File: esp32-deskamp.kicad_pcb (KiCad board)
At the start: 2 copper layers, 145.2 x 66.5 mm, 39 parts, among them J1 INPUT 00, J10 ADDITIONAL GPIO, J2 INPUT 01, J3 MUTE, J4 SLEEP, J5 PRE OUT, J6 LFE OUT, J7 INPUT SELECT, J8 MOTOR, J9 12V IN, K1 INPUT 00, K2 INPUT 01, K3 AMP MUTE, K4 AMP SLEEP, U1 ESP32 D1 MINI, U2 TSR 1-2433, U3 L9110, U4 ULN2003A

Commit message: Update esp32-deskamp.kicad_pcb
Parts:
- moved R7 51.3 mm to (147.5, 74.0), turned to -90 degrees
- moved R8 48.8 mm to (145.2, 74.0), turned to -90 degrees
- moved R9 46.4 mm to (143.0, 74.0), turned to -90 degrees
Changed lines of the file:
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@@
 	(footprint "Resistor_SMD:R_0805_2012Metric_Pad1.20x1.40mm_HandSolder"
 		(layer "F.Cu")
-		(at 96.75 81.75 180)
+		(at 147.5 74 -90)
 		(descr "Resistor SMD 0805 (2012 Metric), square (rectangular) end terminal, IPC-7351 nominal with elongated pad for handsoldering. (Body size source: IPC-SM-782 page 72, https://www.pcb-3d.com/wordpress/wp-content/uploads/ipc-sm-782a_amendment_1_and_2.pdf), generated with kicad-footprint-generator")
 		(tags "resistor handsolder")
 		(property "Reference" "R7"
-			(at 0 -1.65 0)
+			(at 0 -1.65 90)
 			(layer "F.SilkS")
 			(hide yes)
@@
 		)
 		(property "Value" "10K"
-			(at 0 1.875 0)
+			(at 0 1.875 90)
 			(layer "F.SilkS")
 			(hide yes)
@@
 		)
 		(property "Datasheet" ""
-			(at 0 0 0)
+			(at 0 0 90)
 			(layer "F.Fab")
 			(hide yes)
@@
 		)
 		(property "Description" "Resistor"
-			(at 0 0 0)
+			(at 0 0 90)
 			(layer "F.Fab")
 			(hide yes)
@@
 		)
 		(fp_line
-			(start 1.85 0.95)
-			(end -1.85 0.95)
+			(start -1.85 0.95)
+			(end -1.85 -0.95)
 			(stroke
 				(width 0.05)
@@
 		)
 		(fp_line
-			(start 1.85 -0.95)
-			(end 1.85 0.95)
+			(start 1.85 0.95)
+			(end -1.85 0.95)
 			(stroke
 				(width 0.05)
@@
 		)
 		(fp_line
-			(start -1.85 0.95)
-			(end -1.85 -0.95)
+			(start -1.85 -0.95)
+			(end 1.85 -0.95)
 			(stroke
 				(width 0.05)
@@
 		)
 		(fp_line
-			(start -1.85 -0.95)
-			(end 1.85 -0.95)
+			(start 1.85 -0.95)
+			(end 1.85 0.95)
 			(stroke
 				(width 0.05)
@@
 		)
 		(fp_line
-			(start 1 0.625)
-			(end -1 0.625)
+			(start -1 0.625)
+			(end -1 -0.625)
 			(stroke
 				(width 0.1)
@@
 		)
 		(fp_line
-			(start 1 -0.625)
-			(end 1 0.625)
+			(start 1 0.625)
+			(end -1 0.625)
 			(stroke
 				(width 0.1)
@@
 		)
 		(fp_line
-			(start -1 0.625)
-			(end -1 -0.625)
+			(start -1 -0.625)
+			(end 1 -0.625)
 			(stroke
 				(width 0.1)
@@
 		)
 		(fp_line
-			(start -1 -0.625)
-			(end 1 -0.625)
+			(start 1 -0.625)
+			(end 1 0.625)
 			(stroke
 				(width 0.1)
@@
 		)
 		(fp_text user "${REFERENCE}"
-			(at 0 0 0)
+			(at 0 0 90)
 			(layer "F.Fab")
 			(effects
@@
 		)
 		(pad "1" smd roundrect
-			(at -1 0 180)
+			(at -1 0 270)
 			(size 1.2 1.4)
 			(layers "F.Cu" "F.Mask" "F.Paste")
@@
 		)
 		(pad "2" smd roundrect
-			(at 1 0 180)
+			(at 1 0 270)
 			(size 1.2 1.4)
 			(layers "F.Cu" "F.Mask" "F.Paste")
@@
 		(tags "CP Radial series Radial pin pitch 5.00mm diameter 11.5mm supercapacitor")
 		(property "Reference" "C1"
-			(at -5 -1.3025 0)
+			(at 0 2.1975 0)
 			(layer "F.SilkS")
 			(effects
@@
 	(footprint "Resistor_SMD:R_0805_2012Metric_Pad1.20x1.40mm_HandSolder"
 		(layer "F.Cu")
-		(at 96.75 79.5 180)
+		(at 145.25 74 -90)
 		(descr "Resistor SMD 0805 (2012 Metric), square (rectangular) end terminal, IPC-7351 nominal with elongated pad for handsoldering. (Body size source: IPC-SM-782 page 72, https://www.pcb-3d.com/wordpress/wp-content/uploads/ipc-sm-782a_amendment_1_and_2.pdf), generated with kicad-footprint-generator")
 		(tags "resistor handsolder")
 		(property "Reference" "R8"
-			(at 0 -1.65 0)
+			(at 0 -1.65 90)
 			(layer "F.SilkS")
 			(hide yes)
@@
 		)
 		(property "Value" "10K"
-			(at 0 1.875 0)
+			(at 0 1.875 90)
 			(layer "F.SilkS")
 			(hide yes)
@@
 		)
 		(property "Datasheet" ""
-			(at 0 0 0)
+			(at 0 0 90)
 			(layer "F.Fab")
 			(hide yes)
@@
 		)
 		(property "Description" "Resistor"
-			(at 0 0 0)
+			(at 0 0 90)
 			(layer "F.Fab")
 			(hide yes)
@@
 		)
 		(fp_line
-			(start 1.85 0.95)
-			(end -1.85 0.95)
+			(start -1.85 0.95)
+			(end -1.85 -0.95)
 			(stroke
 				(width 0.05)
@@
 		)
 		(fp_line
-			(start 1.85 -0.95)
-			(end 1.85 0.95)
+			(start 1.85 0.95)
+			(end -1.85 0.95)
 			(stroke
 				(width 0.05)
@@
 		)
 		(fp_line
-			(start -1.85 0.95)
-			(end -1.85 -0.95)
+			(start -1.85 -0.95)
+			(end 1.85 -0.95)
 			(stroke
 				(width 0.05)
@@
 		)
 		(fp_line
-			(start -1.85 -0.95)
-			(end 1.85 -0.95)
+			(start 1.85 -0.95)
+			(end 1.85 0.95)
 			(stroke
 				(width 0.05)
@@
 		)
 		(fp_line
-			(start 1 0.625)
-			(end -1 0.625)
+			(start -1 0.625)
+			(end -1 -0.625)
 			(stroke
 				(width 0.1)
@@
 		)
 		(fp_line
-			(start 1 -0.625)
-			(end 1 0.625)
+			(start 1 0.625)
+			(end -1 0.625)
 			(stroke
 				(width 0.1)
@@
 		)
 		(fp_line
-			(start -1 0.625)
-			(end -1 -0.625)
+			(start -1 -0.625)
+			(end 1 -0.625)
 			(stroke
 				(width 0.1)
@@
 		)
 		(fp_line
-			(start -1 -0.625)
-			(end 1 -0.625)
+			(start 1 -0.625)
+			(end 1 0.625)
 			(stroke
 				(width 0.1)
@@
 		)
 		(fp_text user "${REFERENCE}"
-			(at 0 0 0)
+			(at 0 0 90)
 			(layer "F.Fab")
 			(effects
@@
 		)
 		(pad "1" smd roundrect
-			(at -1 0 180)
+			(at -1 0 270)
 			(size 1.2 1.4)
 			(layers "F.Cu" "F.Mask" "F.Paste")
@@
 		)
 		(pad "2" smd roundrect
-			(at 1 0 180)
+			(at 1 0 270)
 			(size 1.2 1.4)
 			(layers "F.Cu" "F.Mask" "F.Paste")
@@
 	(footprint "Resistor_SMD:R_0805_2012Metric_Pad1.20x1.40mm_HandSolder"
 		(layer "F.Cu")
-		(at 96.75 77.25 180)
+		(at 143 74 -90)
 		(descr "Resistor SMD 0805 (2012 Metric), square (rectangular) end terminal, IPC-7351 nominal with elongated pad for handsoldering. (Body size source: IPC-SM-782 page 72, https://www.pcb-3d.com/wordpress/wp-content/uploads/ipc-sm-782a_amendment_1_and_2.pdf), generated with kicad-footprint-generator")
 		(tags "resistor handsolder")
 		(property "Reference" "R9"
-			(at 0 -1.65 0)
+			(at 0 -1.65 90)
 			(layer "F.SilkS")
 			(hide yes)
@@
 		)
 		(property "Value" "10K"
-			(at 2.75 -2 90)
+			(at 2.75 -2 0)
 			(layer "F.SilkS")
 			(effects
@@
 		)
 		(property "Datasheet" ""
-			(at 0 0 0)
+			(at 0 0 90)
 			(layer "F.Fab")
 			(hide yes)
@@
 		)
 		(property "Description" "Resistor"
-			(at 0 0 0)
+			(at 0 0 90)
 			(layer "F.Fab")
 			(hide yes)
@@
 		)
 		(fp_line
-			(start 1.85 0.95)
-			(end -1.85 0.95)
+			(start -1.85 0.95)
+			(end -1.85 -0.95)
 			(stroke
 				(width 0.05)
@@
 		)
 		(fp_line
-			(start 1.85 -0.95)
-			(end 1.85 0.95)
+			(start 1.85 0.95)
+			(end -1.85 0.95)
 			(stroke
 				(width 0.05)
@@
 		)
 		(fp_line
-			(start -1.85 0.95)
-			(end -1.85 -0.95)
+			(start -1.85 -0.95)
+			(end 1.85 -0.95)
 			(stroke
 				(width 0.05)
@@
 		)
 		(fp_line
-			(start -1.85 -0.95)
-			(end 1.85 -0.95)
+			(start 1.85 -0.95)
+			(end 1.85 0.95)
 			(stroke
 				(width 0.05)
@@
 		)
 		(fp_line
-			(start 1 0.625)
-			(end -1 0.625)
+			(start -1 0.625)
+			(end -1 -0.625)
 			(stroke
 				(width 0.1)
@@
 		)
 		(fp_line
-			(start 1 -0.625)
-			(end 1 0.625)
+			(start 1 0.625)
+			(end -1 0.625)
 			(stroke
 				(width 0.1)
@@
 		)
 		(fp_line
-			(start -1 0.625)
-			(end -1 -0.625)
+			(start -1 -0.625)
+			(end 1 -0.625)
 			(stroke
 				(width 0.1)
@@
 		)
 		(fp_line
-			(start -1 -0.625)
-			(end 1 -0.625)
+			(start 1 -0.625)
+			(end 1 0.625)
 			(stroke
 				(width 0.1)
@@
 		)
 		(fp_text user "${REFERENCE}"
-			(at 0 0 0)
+			(at 0 0 90)
 			(layer "F.Fab")
 			(effects
@@
 		)
 		(pad "1" smd roundrect
-			(at -1 0 180)
+			(at -1 0 270)
 			(size 1.2 1.4)
 			(layers "F.Cu" "F.Mask" "F.Paste")
@@
 		)
 		(pad "2" smd roundrect
-			(at 1 0 180)
+			(at 1 0 270)
 			(size 1.2 1.4)
 			(layers "F.Cu" "F.Mask" "F.Paste")

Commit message: Moar layout
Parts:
- R7, R8, R9: footprint Resistor_SMD:R_0805_2012Metric_Pad1.20x1.40mm_HandSolder -> Resistor_THT:R_Axial_DIN0204_L3.6mm_D1.6mm_P5.08mm_Horizontal
- U4: footprint Package_SO:SSOP-16_4.4x5.2mm_P0.65mm -> Package_DIP:DIP-16_W7.62mm
- moved J10 103.5 mm to (73.7, 154.0)
- moved J7 60.0 mm to (152.8, 93.5)
- moved U1 42.5 mm to (107.0, 82.8), turned to 90 degrees
- moved J8 40.8 mm to (161.8, 93.5)
- moved U3 40.5 mm to (152.9, 81.6), turned to 90 degrees
- moved R8 23.6 mm to (135.0, 95.2), turned to 0 degrees
- moved C1 21.3 mm to (95.2, 59.1)
- moved R7 20.5 mm to (135.0, 90.2), turned to 0 degrees
- moved R9 20.4 mm to (135.0, 92.8), turned to 0 degrees
- moved ? 19.3 mm to (129.2, 96.5)
- moved REF** 19.2 mm to (129.2, 96.2)
- moved U4 17.5 mm to (142.8, 70.5)
- moved U2 10.8 mm to (113.7, 63.8)
- moved ? 0.50 mm to (100.2, 38.5) (x2)
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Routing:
- net Relay2: track 52.6 -> 4.27 mm, vias 1 -> 0
- net Input1: track 38.0 -> 0.00 mm, vias 1 -> 0
- net Input0: track 37.4 -> 0.00 mm, vias 1 -> 0
- net Sleep: track 36.6 -> 0.00 mm, vias 1 -> 0
- net Mute: track 36.2 -> 0.00 mm, vias 1 -> 0
- net PWM1: track 34.9 -> 0.00 mm
- net PWM0: track 32.9 -> 0.00 mm
- net Relay1: track 36.4 -> 4.13 mm, vias 1 -> 0
- net Relay3: track 26.4 -> 4.32 mm, vias 1 -> 0
- net Net-(J8-Pin_2): track 20.1 -> 0.00 mm
- net +3V3: track 41.4 -> 58.1 mm
- net +12V: track 148.3 -> 132.9 mm
- net Relay0: track 18.1 -> 4.00 mm, vias 1 -> 0
- net Net-(J8-Pin_1): track 12.0 -> 0.00 mm
- net Select2: track 0.00 -> 11.6 mm
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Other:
- outline, holes or cut-outs redrawn

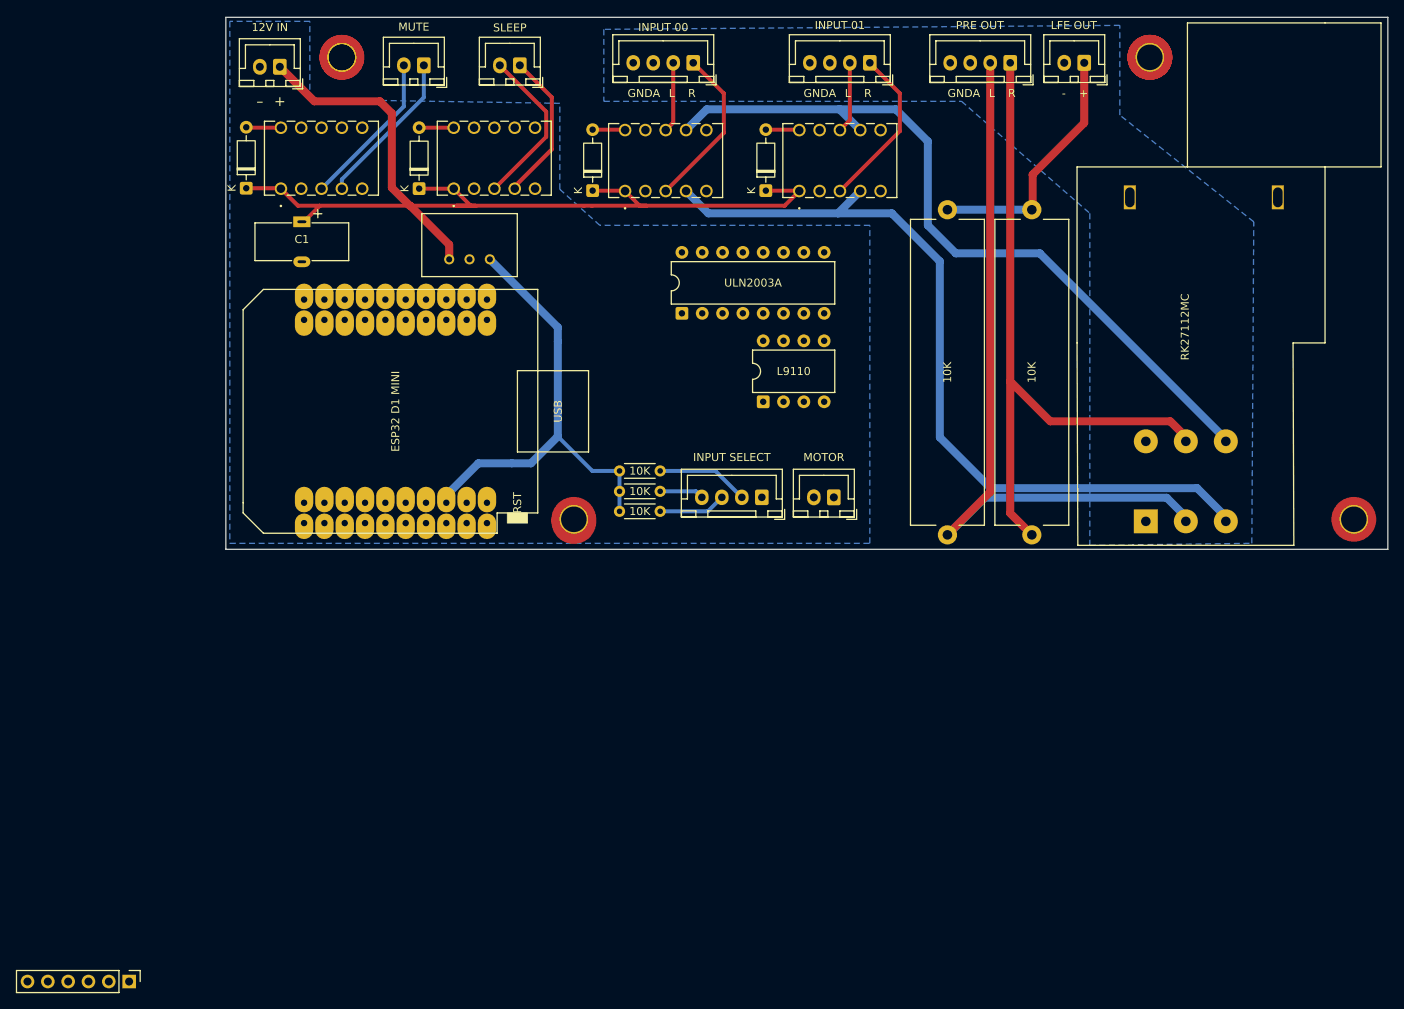
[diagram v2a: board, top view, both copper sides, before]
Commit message: Fix cap footprint, moar layout
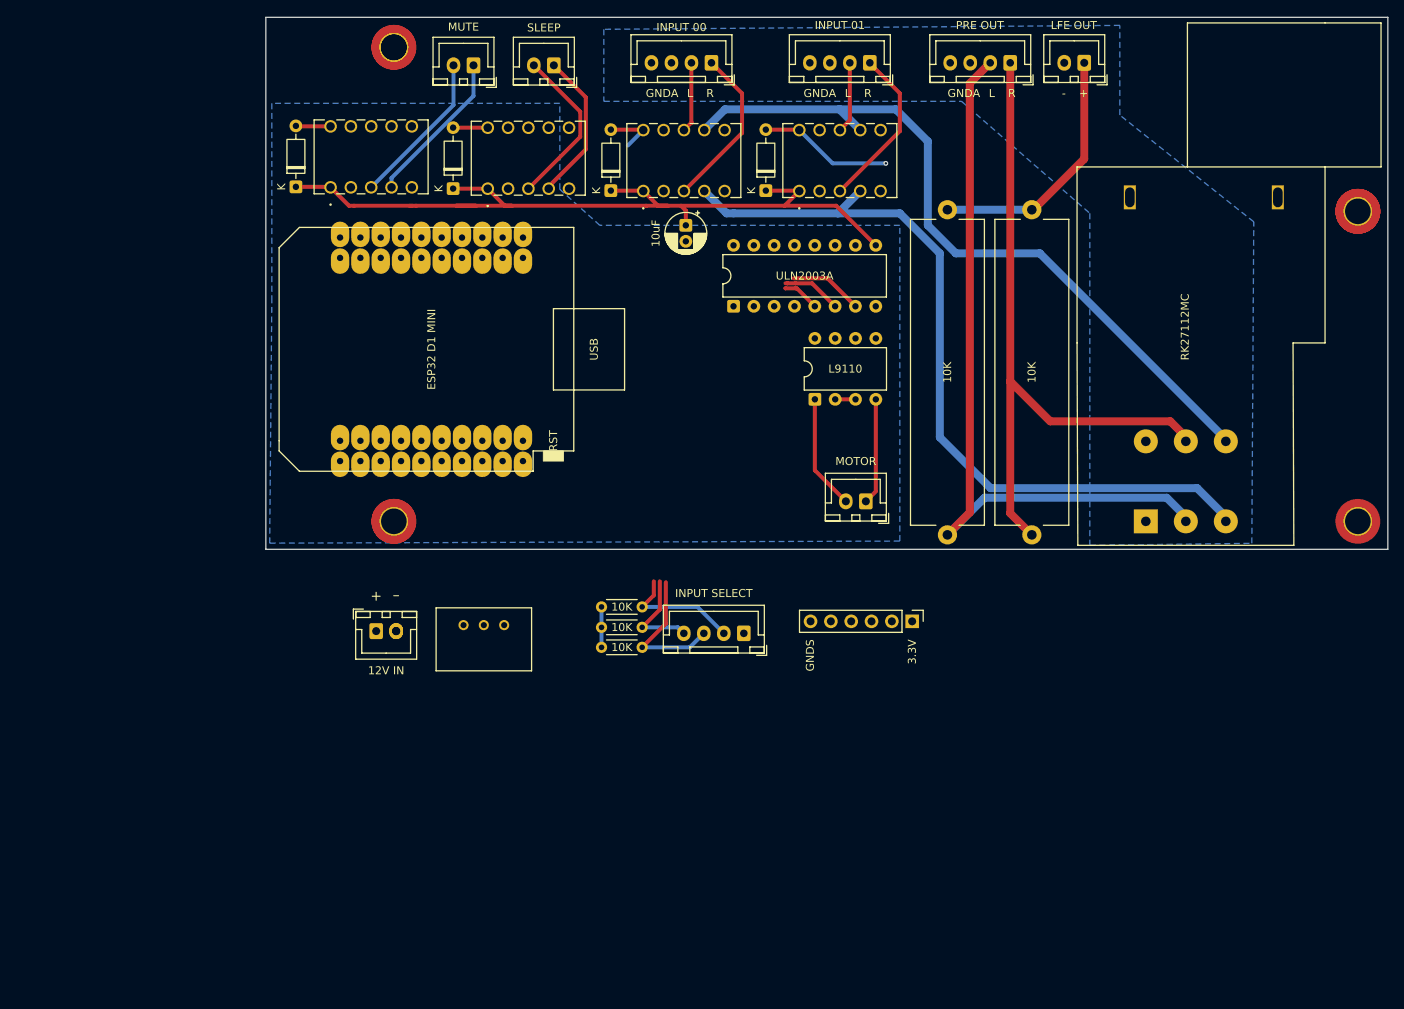
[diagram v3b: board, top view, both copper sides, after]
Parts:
- added ?: , , F.Cu at (107.0, 110.2)
- C1: footprint Capacitor_THT:DX_5R5VxxxxU_D11.5mm_P5.00mm -> Capacitor_THT:CP_Radial_D5.0mm_P2.00mm
- moved J10 107.7 mm to (171.5, 109.0)
- moved J9 71.6 mm to (104.5, 110.2), turned to 0 degrees
- moved C1 48.0 mm to (143.2, 59.5), turned to -90 degrees
- moved U2 46.2 mm to (120.5, 109.5), turned to 180 degrees
- moved ? 32.4 mm to (227.2, 57.8) (x3)
- moved REF** 32.4 mm to (227.2, 57.8)
- moved REF** 22.5 mm to (106.8, 96.5)
- moved ? 22.5 mm to (106.8, 96.5)
- moved J7 17.1 mm to (150.5, 110.5)
- moved R7 17.1 mm to (132.7, 107.2)
- moved R8 17.1 mm to (132.7, 112.2)
- moved R9 17.1 mm to (132.7, 109.8)
- moved U1 8.96 mm to (111.5, 75.0)
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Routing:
- net +3V3: track 58.1 -> 7.59 mm
- net +12V: track 132.9 -> 103.4 mm
- net Net-(J8-Pin_2): track 0.00 -> 14.4 mm
- net Net-(J8-Pin_1): track 0.00 -> 13.3 mm
- net Relay1: track 4.13 -> 16.7 mm, vias 0 -> 1
- net Select1: track 8.43 -> 17.8 mm
- net Input1: track 0.00 -> 9.20 mm
- net Input0: track 0.00 -> 7.40 mm
- net Select0: track 5.52 -> 12.2 mm
- net Sleep: track 0.00 -> 4.60 mm
- net Select2: track 11.6 -> 15.4 mm
- net Relay0: track 4.00 -> 6.74 mm
- net PRE_LEFT: track 96.2 -> 93.7 mm
- net GNDA: track 2.26 -> 0.00 mm
- net PRE_RIGHT: track 102.1 -> 100.4 mm
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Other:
- board size 145.2 x 66.5 mm -> 140.2 x 66.5 mm
- board text added: "3.3V"
- board text added: "GNDS"

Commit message: Almost there, V3-something.
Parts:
- moved ? 71.7 mm to (98.5, 39.0)
- moved J9 71.7 mm to (96.0, 39.0)
- moved U2 46.1 mm to (139.7, 67.5), turned to -90 degrees
- moved J10 43.0 mm to (130.8, 95.0), turned to 90 degrees
- moved R8 37.5 mm to (151.5, 79.8), turned to -90 degrees
- moved R7 34.7 mm to (154.0, 79.8), turned to -90 degrees
- moved R9 34.1 mm to (149.0, 79.8), turned to -90 degrees
- moved J7 17.6 mm to (156.5, 94.0)
- moved U1 1.68 mm to (111.5, 76.7)
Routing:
- net +12V: track 103.4 -> 186.2 mm
- net Select1: track 17.8 -> 8.46 mm
- net Relay1: track 16.7 -> 7.58 mm
- net Select2: track 15.4 -> 8.46 mm
- net +3V3: track 7.59 -> 2.54 mm
- net Select0: track 12.2 -> 8.46 mm
- net Relay0: track 6.74 -> 4.00 mm

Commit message: Update esp32-deskamp.kicad_pcb
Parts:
- removed the ? at (98.5, 39.0)
- moved J9 2.55 mm to (98.5, 39.5), turned to 180 degrees
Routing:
- net +3V3: track 2.54 -> 46.4 mm

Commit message: IC routing
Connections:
- U1 pad 25: Input1 -> Mute
- U1 pad 31: Mute -> Input1
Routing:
- net Select0: track 8.46 -> 58.9 mm
- net Select1: track 8.46 -> 58.8 mm
- net Select2: track 8.46 -> 58.8 mm
- net +3V3: track 46.4 -> 83.7 mm
- net Mute: track 0.00 -> 24.6 mm, vias 0 -> 1
- net Input1: track 9.20 -> 33.2 mm, vias 0 -> 1
- net Input0: track 7.40 -> 31.2 mm, vias 0 -> 1
- net Sleep: track 4.60 -> 27.7 mm, vias 0 -> 1
- net +12V: track 185.9 -> 180.0 mm
- net PWM1: track 0.00 -> 0.57 mm
- net PWM0: track 0.00 -> 0.57 mm
